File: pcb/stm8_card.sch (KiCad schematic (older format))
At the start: 21 parts

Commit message: pcb capitalized stm8s103f3
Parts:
- U?: value stm8s103f3 -> STM8S103F3; symbol stm8_card:stm8s103f3 -> stm8_card:STM8S103F3
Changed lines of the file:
@@
 $EndDescr
 $Comp
-L stm8_card:stm8s103f3 U?
+L stm8_card:STM8S103F3 U?
 U 1 1 60826CD3
 P 8100 3000
 F 0 "U?" H 8400 3750 50  0000 C CNN
-F 1 "stm8s103f3" H 8400 3650 50  0000 C CNN
+F 1 "STM8S103F3" H 8400 3650 50  0000 C CNN
 F 2 "" H 8500 3000 50  0001 C CNN
 F 3 "~" H 8500 3000 50  0001 C CNN

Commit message: pcb improved schematic
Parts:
- added C5: 1uf, symbol Device:C_Small
- C4: renamed from C?; value 1uf -> 22nf
- R1: renamed from R?; value 4.7k -> 390k
- U2: renamed from U?; footprint (none) -> Package_SO:TSSOP-20_4.4x6.5mm_P0.65mm
- gave numbers to parts that had none: 18
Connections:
- net 3v3: now also C5.2
- net GND: now also BT1.2 (-), C5.1
- no-connect marks 0 -> 10
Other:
- moved on the sheet: C4, C8, SW4

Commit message: pcb created and assigned oled footprint
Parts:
- U1: footprint (none) -> stm8_card:ER-OLED0.91-7
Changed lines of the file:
@@
 F 0 "U1" H 2800 2850 50  0000 C CNN
 F 1 "ER-OLED0.91-7" H 2850 2750 50  0000 C CNN
-F 2 "" H 1000 2500 50  0001 C CNN
+F 2 "stm8_card:ER-OLED0.91-7" H 1000 2500 50  0001 C CNN
 F 3 "" H 1000 2500 50  0001 C CNN
 	1    2500 2100

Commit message: pcb added 0805 handsolder footprints to C and R
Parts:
- C1, C2, C3, C4, C5, C6, C7, C8: footprint (none) -> Capacitor_SMD:C_0805_2012Metric_Pad1.18x1.45mm_HandSolder
- R1, R2, R3, R4, R5, R6: footprint (none) -> Resistor_SMD:R_0805_2012Metric_Pad1.20x1.40mm_HandSolder
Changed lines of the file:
@@
 F 0 "R4" V 4500 4050 50  0000 C CNN
 F 1 "4.7k" V 4600 4050 50  0000 C CNN
-F 2 "" V 4530 4050 50  0001 C CNN
+F 2 "Resistor_SMD:R_0805_2012Metric_Pad1.20x1.40mm_HandSolder" V 4530 4050 50  0001 C CNN
 F 3 "~" H 4600 4050 50  0001 C CNN
 	1    4600 4050
@@
 F 0 "R5" V 4500 4500 50  0000 C CNN
 F 1 "4.7k" V 4600 4500 50  0000 C CNN
-F 2 "" V 4530 4500 50  0001 C CNN
+F 2 "Resistor_SMD:R_0805_2012Metric_Pad1.20x1.40mm_HandSolder" V 4530 4500 50  0001 C CNN
 F 3 "~" H 4600 4500 50  0001 C CNN
 	1    4600 4500
@@
 F 0 "R6" V 4500 4950 50  0000 C CNN
 F 1 "4.7k" V 4600 4950 50  0000 C CNN
-F 2 "" V 4530 4950 50  0001 C CNN
+F 2 "Resistor_SMD:R_0805_2012Metric_Pad1.20x1.40mm_HandSolder" V 4530 4950 50  0001 C CNN
 F 3 "~" H 4600 4950 50  0001 C CNN
 	1    4600 4950
@@
 F 0 "C1" H 1492 1896 50  0000 L CNN
 F 1 "1uf" H 1492 1805 50  0000 L CNN
-F 2 "" H 1400 1850 50  0001 C CNN
+F 2 "Capacitor_SMD:C_0805_2012Metric_Pad1.18x1.45mm_HandSolder" H 1400 1850 50  0001 C CNN
 F 3 "~" H 1400 1850 50  0001 C CNN
 	1    1400 1850
@@
 F 0 "C2" H 1492 2196 50  0000 L CNN
 F 1 "1uf" H 1492 2105 50  0000 L CNN
-F 2 "" H 1400 2150 50  0001 C CNN
+F 2 "Capacitor_SMD:C_0805_2012Metric_Pad1.18x1.45mm_HandSolder" H 1400 2150 50  0001 C CNN
 F 3 "~" H 1400 2150 50  0001 C CNN
 	1    1400 2150
@@
 F 0 "R3" V 4050 2700 50  0000 C CNN
 F 1 "4.7k" V 3950 2700 50  0000 C CNN
-F 2 "" V 3880 2700 50  0001 C CNN
+F 2 "Resistor_SMD:R_0805_2012Metric_Pad1.20x1.40mm_HandSolder" V 3880 2700 50  0001 C CNN
 F 3 "~" H 3950 2700 50  0001 C CNN
 	1    3950 2700
@@
 F 0 "R2" V 3750 2700 50  0000 C CNN
 F 1 "4.7k" V 3650 2700 50  0000 C CNN
-F 2 "" V 3580 2700 50  0001 C CNN
+F 2 "Resistor_SMD:R_0805_2012Metric_Pad1.20x1.40mm_HandSolder" V 3580 2700 50  0001 C CNN
 F 3 "~" H 3650 2700 50  0001 C CNN
 	1    3650 2700
@@
 F 0 "R1" V 3350 2200 50  0000 C CNN
 F 1 "390k" V 3300 2050 50  0000 C CNN
-F 2 "" V 3230 2050 50  0001 C CNN
+F 2 "Resistor_SMD:R_0805_2012Metric_Pad1.20x1.40mm_HandSolder" V 3230 2050 50  0001 C CNN
 F 3 "~" H 3300 2050 50  0001 C CNN
 	1    3300 2050
@@
 F 0 "C7" V 3250 1800 50  0000 C CNN
 F 1 "4.7uf" V 3250 2050 50  0000 C CNN
-F 2 "" H 3300 1900 50  0001 C CNN
+F 2 "Capacitor_SMD:C_0805_2012Metric_Pad1.18x1.45mm_HandSolder" H 3300 1900 50  0001 C CNN
 F 3 "~" H 3300 1900 50  0001 C CNN
 	1    3300 1900
@@
 F 0 "C6" V 3250 1650 50  0000 C CNN
 F 1 "2.2uf" V 3250 1900 50  0000 C CNN
-F 2 "" H 3300 1750 50  0001 C CNN
+F 2 "Capacitor_SMD:C_0805_2012Metric_Pad1.18x1.45mm_HandSolder" H 3300 1750 50  0001 C CNN
 F 3 "~" H 3300 1750 50  0001 C CNN
 	1    3300 1750
@@
 F 0 "C4" H 1850 3000 50  0000 L CNN
 F 1 "22nf" H 1850 2800 50  0000 L CNN
-F 2 "" H 1800 2900 50  0001 C CNN
+F 2 "Capacitor_SMD:C_0805_2012Metric_Pad1.18x1.45mm_HandSolder" H 1800 2900 50  0001 C CNN
 F 3 "~" H 1800 2900 50  0001 C CNN
 	1    1800 2900
@@
 F 0 "C3" H 1550 3000 50  0000 L CNN
 F 1 "1uf" H 1550 2800 50  0000 L CNN
-F 2 "" H 1500 2900 50  0001 C CNN
+F 2 "Capacitor_SMD:C_0805_2012Metric_Pad1.18x1.45mm_HandSolder" H 1500 2900 50  0001 C CNN
 F 3 "~" H 1500 2900 50  0001 C CNN
 	1    1500 2900
@@
 F 0 "C8" H 7192 3646 50  0000 L CNN
 F 1 "1uf" H 7192 3555 50  0000 L CNN
-F 2 "" H 7100 3600 50  0001 C CNN
+F 2 "Capacitor_SMD:C_0805_2012Metric_Pad1.18x1.45mm_HandSolder" H 7100 3600 50  0001 C CNN
 F 3 "~" H 7100 3600 50  0001 C CNN
 	1    7100 3600
@@
 F 0 "C5" V 2300 1350 50  0000 L CNN
 F 1 "1uf" V 2300 1100 50  0000 L CNN
-F 2 "" H 2250 1300 50  0001 C CNN
+F 2 "Capacitor_SMD:C_0805_2012Metric_Pad1.18x1.45mm_HandSolder" H 2250 1300 50  0001 C CNN
 F 3 "~" H 2250 1300 50  0001 C CNN
 	1    2250 1300

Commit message: pcb debug icsp footprint
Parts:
- J1: footprint (none) -> stm8_card:2mm_2x4_ICSP
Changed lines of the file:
@@
 F 0 "J1" H 5330 1642 50  0000 L CNN
 F 1 "DEBUG HEADER" H 5330 1551 50  0000 L CNN
-F 2 "" H 5250 1650 50  0001 C CNN
+F 2 "stm8_card:2mm_2x4_ICSP" H 5250 1650 50  0001 C CNN
 F 3 "~" H 5250 1650 50  0001 C CNN
 	1    5250 1650

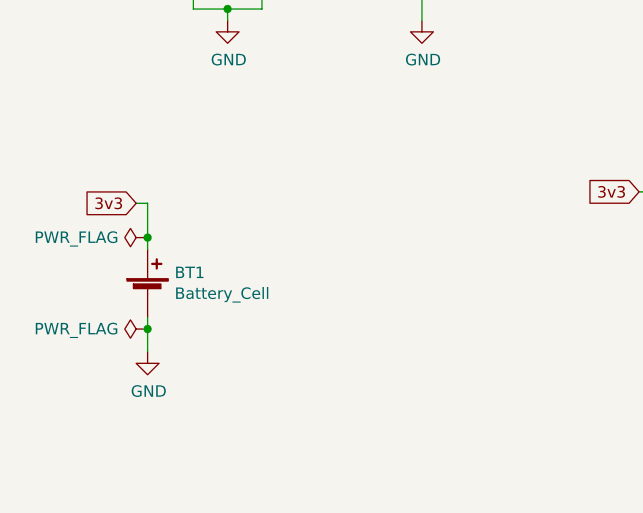
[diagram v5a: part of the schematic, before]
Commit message: pcb footprint for eg4378ct-nd
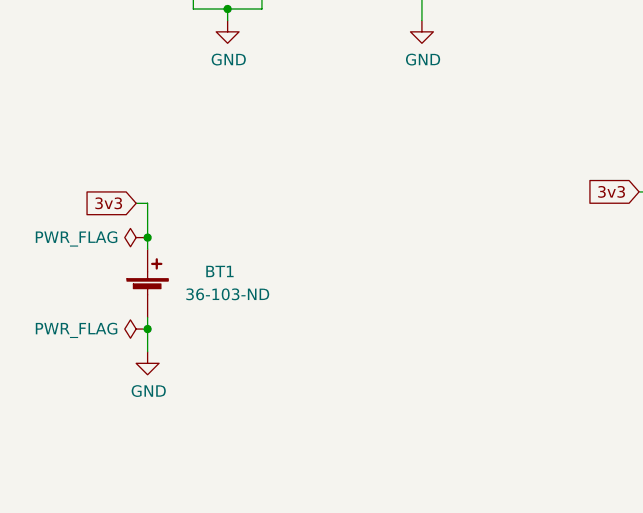
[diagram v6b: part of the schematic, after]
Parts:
- BT1: value Battery_Cell -> 103; footprint (none) -> Battery:BatteryHolder_Keystone_103_1x20mm; digikey (none) -> 36-103-ND
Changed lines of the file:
@@
 U 1 1 6081E543
 P 1300 4400
-F 0 "BT1" H 1418 4496 50  0000 L CNN
-F 1 "Battery_Cell" H 1418 4405 50  0000 L CNN
-F 2 "" V 1300 4460 50  0001 C CNN
+F 0 "BT1" H 1550 4500 50  0000 L CNN
+F 1 "103" H 1418 4405 50  0001 L CNN
+F 2 "Battery:BatteryHolder_Keystone_103_1x20mm" V 1300 4460 50  0001 C CNN
 F 3 "~" V 1300 4460 50  0001 C CNN
+F 4 "36-103-ND" H 1650 4400 50  0000 C CNN "digikey"
 	1    1300 4400
 	1    0    0    -1

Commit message: pcb reset button footprint
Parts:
- SW4: footprint (none) -> stm8_card:TL3302AF260QG
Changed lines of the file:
@@
 F 0 "SW4" H 6300 4900 50  0000 C CNN
 F 1 "TL3302AF260QG" H 6300 4884 50  0001 C CNN
-F 2 "" H 6300 4800 50  0001 C CNN
+F 2 "stm8_card:TL3302AF260QG" H 6300 4800 50  0001 C CNN
 F 3 "~" H 6300 4800 50  0001 C CNN
 F 4 "EG4584CT-ND" H 6300 4794 50  0000 C CNN "digikey"

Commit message: pcb actually applied sw footprints
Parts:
- SW1, SW2, SW3: footprint (none) -> stm8_card:TL59AF100Q
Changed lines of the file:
@@
 F 0 "SW1" H 3950 4335 50  0000 C CNN
 F 1 "TL59AF100Q" H 3950 4334 50  0001 C CNN
-F 2 "" H 3950 4250 50  0001 C CNN
+F 2 "stm8_card:TL59AF100Q" H 3950 4250 50  0001 C CNN
 F 3 "~" H 3950 4250 50  0001 C CNN
 F 4 "EG4378CT-ND" H 3950 4244 50  0000 C CNN "digikey"
@@
 F 0 "SW3" H 3950 5235 50  0000 C CNN
 F 1 "TL59AF100Q" H 3950 5234 50  0001 C CNN
-F 2 "" H 3950 5150 50  0001 C CNN
+F 2 "stm8_card:TL59AF100Q" H 3950 5150 50  0001 C CNN
 F 3 "~" H 3950 5150 50  0001 C CNN
 F 4 "EG4378CT-ND" H 3950 5144 50  0000 C CNN "digikey"
@@
 F 0 "SW2" H 3950 4785 50  0000 C CNN
 F 1 "TL59AF100Q" H 3950 4784 50  0001 C CNN
-F 2 "" H 3950 4700 50  0001 C CNN
+F 2 "stm8_card:TL59AF100Q" H 3950 4700 50  0001 C CNN
 F 3 "~" H 3950 4700 50  0001 C CNN
 F 4 "EG4378CT-ND" H 3950 4694 50  0000 C CNN "digikey"
